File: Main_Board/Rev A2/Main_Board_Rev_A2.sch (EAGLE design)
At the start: 209 parts, among them J1 90814-0208, J12 22-27-2061-06, J15 1241050-5, J2 90814-0206, J3 90814-0208, J4 5504F1-09S-02A-03, J5 22-05-7048-04, J6 22-05-7048-04, J7 22-05-7058-05, J8 22-05-7048-04, J9 22-05-7028-02, K1 G6K-2G-Y, K2 G6K-2G-Y, K3 G6K-2G-Y, K4 G6K-2G-Y, P1 RB1-125BAG1A, SW1 B3FS-1050, SW2 B3FS-1050, T2 MMBT2907ALT3, U1 LT3686HDDPBF, U10 SN74LVC2G17DBVR, U11 MCP2561-E/SN, U12 TLV313, U2 TPL0401A, U3 SN74LVC3G17DCTR, U4 SN74LVC3G17DCTR, U5 LT3686HDDPBF, U6 LPC1768FBD100, U7 AT24C512C-SSHM-B, U8 SN74LVC3G17DCTR, U9 SN74LVC2G17DBVR, X1 ASE_50, X12 22-05-7028-02, X13 22-05-7028-02, X14 22-05-7038-03, X15 22-05-7038-03, X2 FC-135, X3 ASE-12, X4 MSTBA2, X5 22-05-7028-02, X6 USB3075-30-A, X7 3000, X8 22-05-7028-02

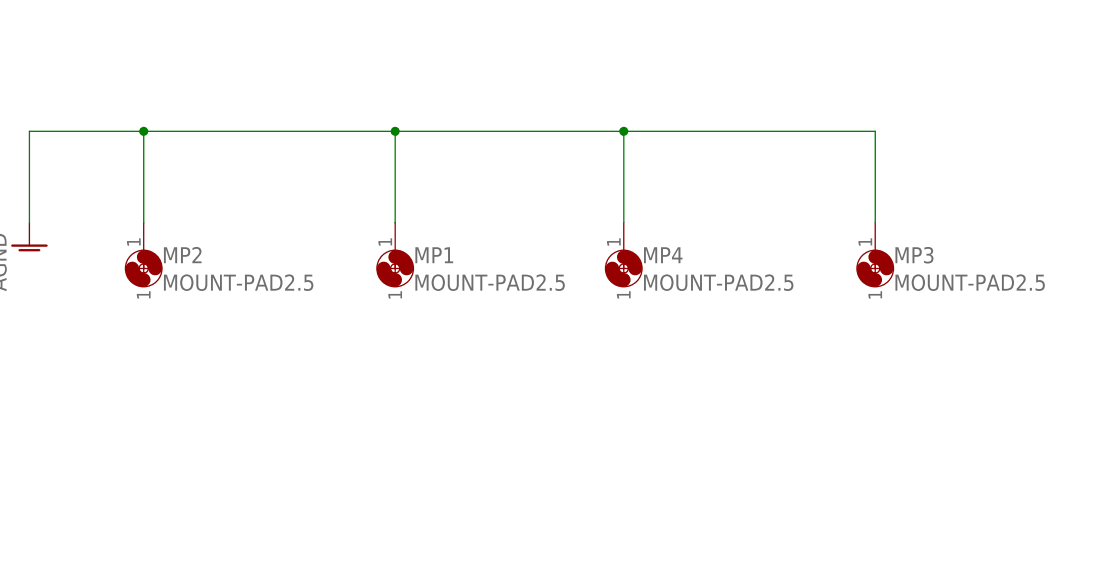
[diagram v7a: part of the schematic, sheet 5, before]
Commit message: Replace mounting hole M2.5 to M3 and add guard ring on inner layer
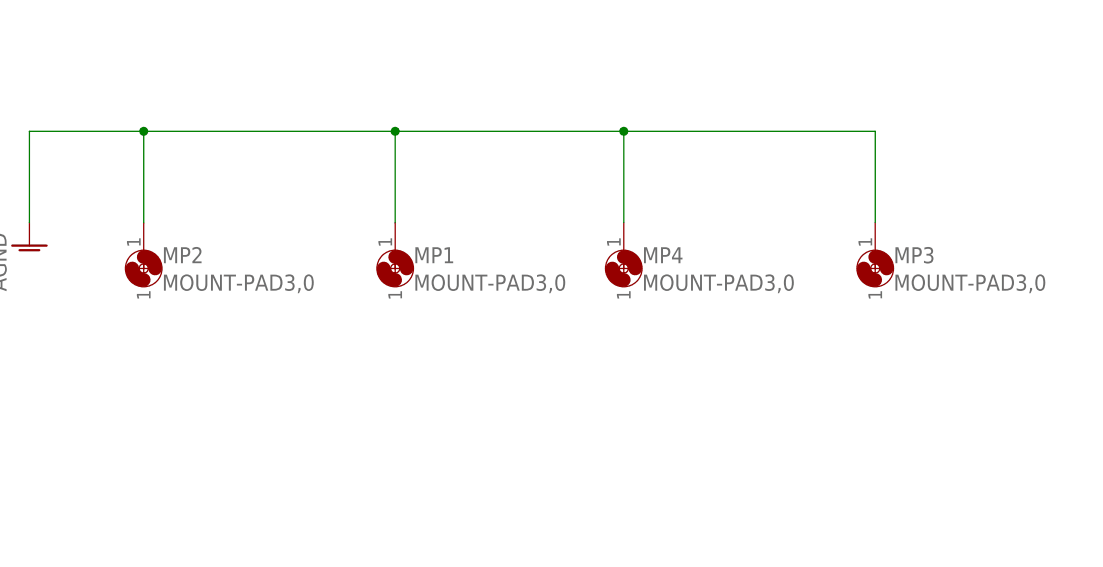
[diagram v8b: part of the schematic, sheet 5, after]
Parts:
- MP1, MP2, MP3, MP4: value MOUNT-PAD2.5 -> MOUNT-PAD3,0; device holes:MOUNT-PAD2.5 -> holes:MOUNT-PAD3,0
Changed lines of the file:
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@@
 <part name="GND80" library="supply1" deviceset="GND" device=""/>
 <part name="P+22" library="supply1" deviceset="+5V" device=""/>
-<part name="MP2" library="holes" deviceset="MOUNT-PAD" device="2.5">
+<part name="MP2" library="holes" deviceset="MOUNT-PAD" device="3,0" value="MOUNT-PAD3,0">
 <attribute name="MF" value=""/>
 <attribute name="MPN" value=""/>
 <attribute name="OC_NEWARK" value="unknown"/>
 </part>
-<part name="MP1" library="holes" deviceset="MOUNT-PAD" device="2.5">
+<part name="MP1" library="holes" deviceset="MOUNT-PAD" device="3,0" value="MOUNT-PAD3,0">
 <attribute name="MF" value=""/>
 <attribute name="MPN" value=""/>
 <attribute name="OC_NEWARK" value="unknown"/>
 </part>
-<part name="MP4" library="holes" deviceset="MOUNT-PAD" device="2.5">
+<part name="MP4" library="holes" deviceset="MOUNT-PAD" device="3,0" value="MOUNT-PAD3,0">
 <attribute name="MF" value=""/>
 <attribute name="MPN" value=""/>
 <attribute name="OC_NEWARK" value="unknown"/>
 </part>
-<part name="MP3" library="holes" deviceset="MOUNT-PAD" device="2.5">
+<part name="MP3" library="holes" deviceset="MOUNT-PAD" device="3,0" value="MOUNT-PAD3,0">
 <attribute name="MF" value=""/>
 <attribute name="MPN" value=""/>
